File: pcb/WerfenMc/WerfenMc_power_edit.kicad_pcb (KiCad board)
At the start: 2 copper layers, 72 x 57 mm, 71 parts, among them J1 MOTOR, J2 SWD, J3 POWER, J4 UART3, J5 UART1, J6 PowerTerminal, Q1 Q_Photo_NPN, Q2 BCP56, SW1 RESET, SW2 ESTOP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

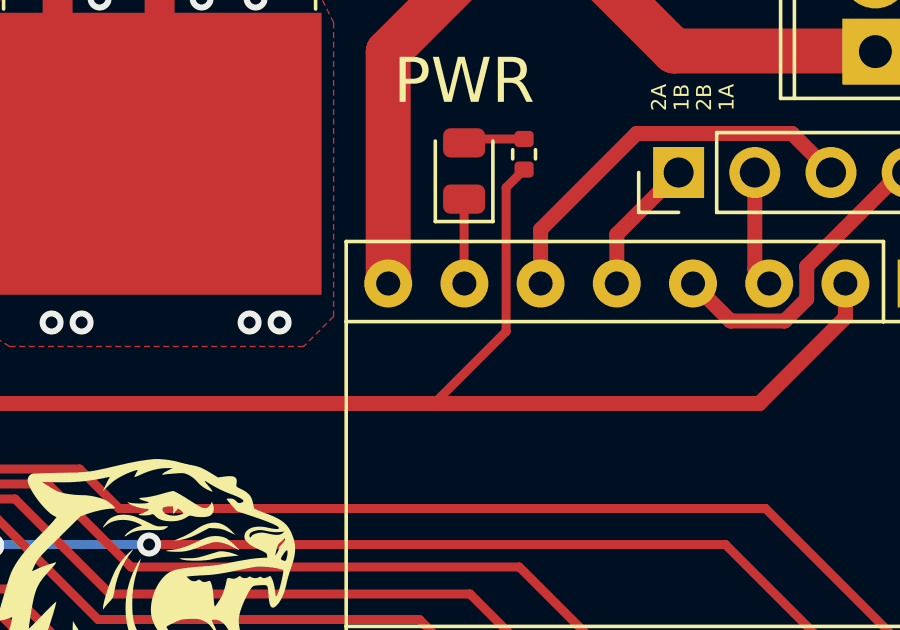
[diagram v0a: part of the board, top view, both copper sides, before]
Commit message: Added a via to motor driver ground, exported better step file
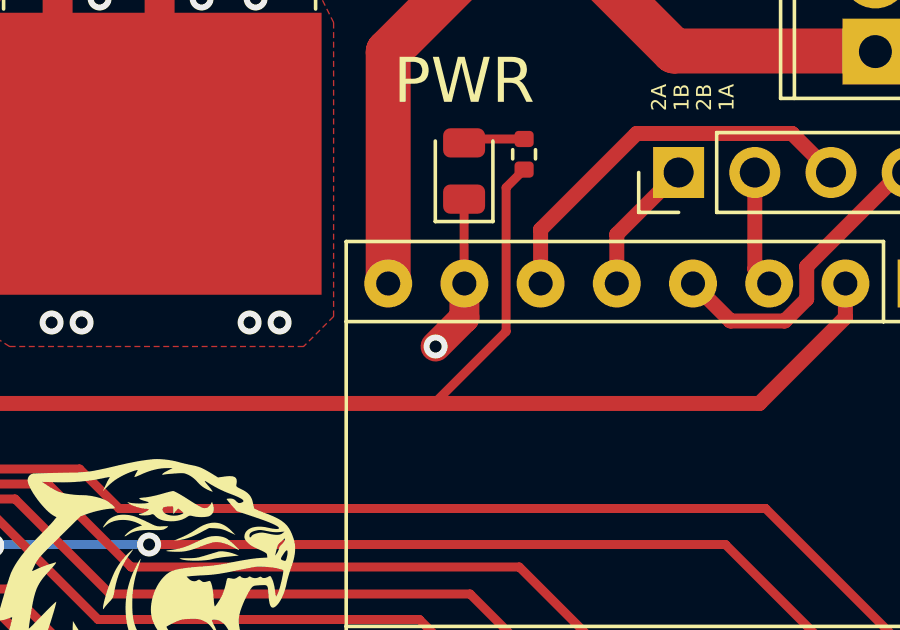
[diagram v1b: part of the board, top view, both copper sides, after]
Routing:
- net GND: track 110.5 -> 112.9 mm, vias 51 -> 52
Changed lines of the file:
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@@
   (segment (start 55.0452 64.1832) (end 52.9293 64.1832) (width 0.3) (layer "F.Cu") (net 1))
   (segment (start 49.785 38.215) (end 51 37) (width 0.3) (layer "F.Cu") (net 1))
+  (segment (start 86.76 54.5) (end 86.76 55.64) (width 1) (layer "F.Cu") (net 1))
   (segment (start 35 59.38) (end 35 57) (width 0.3) (layer "F.Cu") (net 1))
   (segment (start 63.9702 69.0298) (end 63.72 69.28) (width 0.3) (layer "F.Cu") (net 1))
@@
   (segment (start 68.9625 50.175) (end 76.6 50.175) (width 0.3) (layer "F.Cu") (net 1))
   (segment (start 54.65 81) (end 54.65 79.65) (width 0.5) (layer "F.Cu") (net 1))
+  (segment (start 86.76 55.64) (end 85.8 56.6) (width 1) (layer "F.Cu") (net 1))
   (segment (start 57.1 69.5) (end 57.1 70.28) (width 0.3) (layer "F.Cu") (net 1))
   (segment (start 100.46 44.23) (end 100.46 41.46) (width 1.5) (layer "F.Cu") (net 1))
@@
   (via (at 94.2 30) (size 0.8) (drill 0.4) (layers "F.Cu" "B.Cu") (free) (net 1))
   (via (at 89.6 28.6) (size 0.8) (drill 0.4) (layers "F.Cu" "B.Cu") (free) (net 1))
+  (via (at 85.8 56.6) (size 0.8) (drill 0.4) (layers "F.Cu" "B.Cu") (net 1))
   (via (at 55.5 37.2) (size 0.8) (drill 0.4) (layers "F.Cu" "B.Cu") (free) (net 1))
   (via (at 85.6 31.2) (size 0.8) (drill 0.4) (layers "F.Cu" "B.Cu") (free) (net 1))
